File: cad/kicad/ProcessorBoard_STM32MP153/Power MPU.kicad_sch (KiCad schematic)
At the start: 37 parts, among them IC301 STPMIC1BPQR, J301 Conn_01x01_Pin

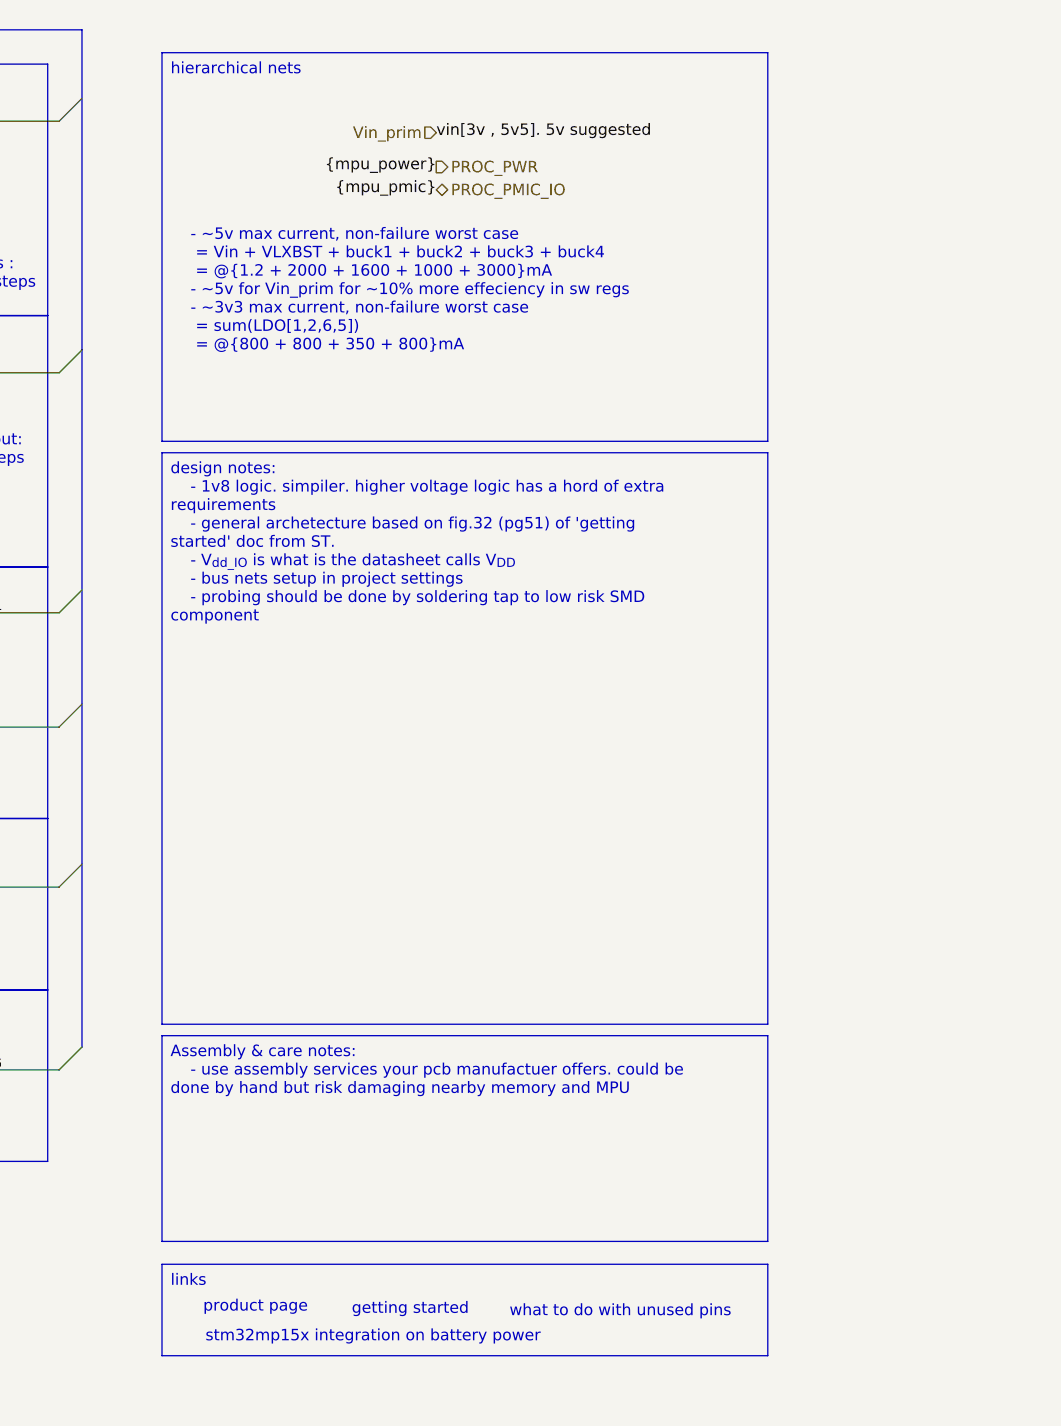
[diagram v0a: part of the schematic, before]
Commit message: realtek bridge thing somewhat more wired
apparently the proper term for via skimping and what not is NFPR (non functional pad removal). all my homies love NFPR. so it is possible to route 0.5mm bga. still fighting the dog but at least cant bring it to another layer
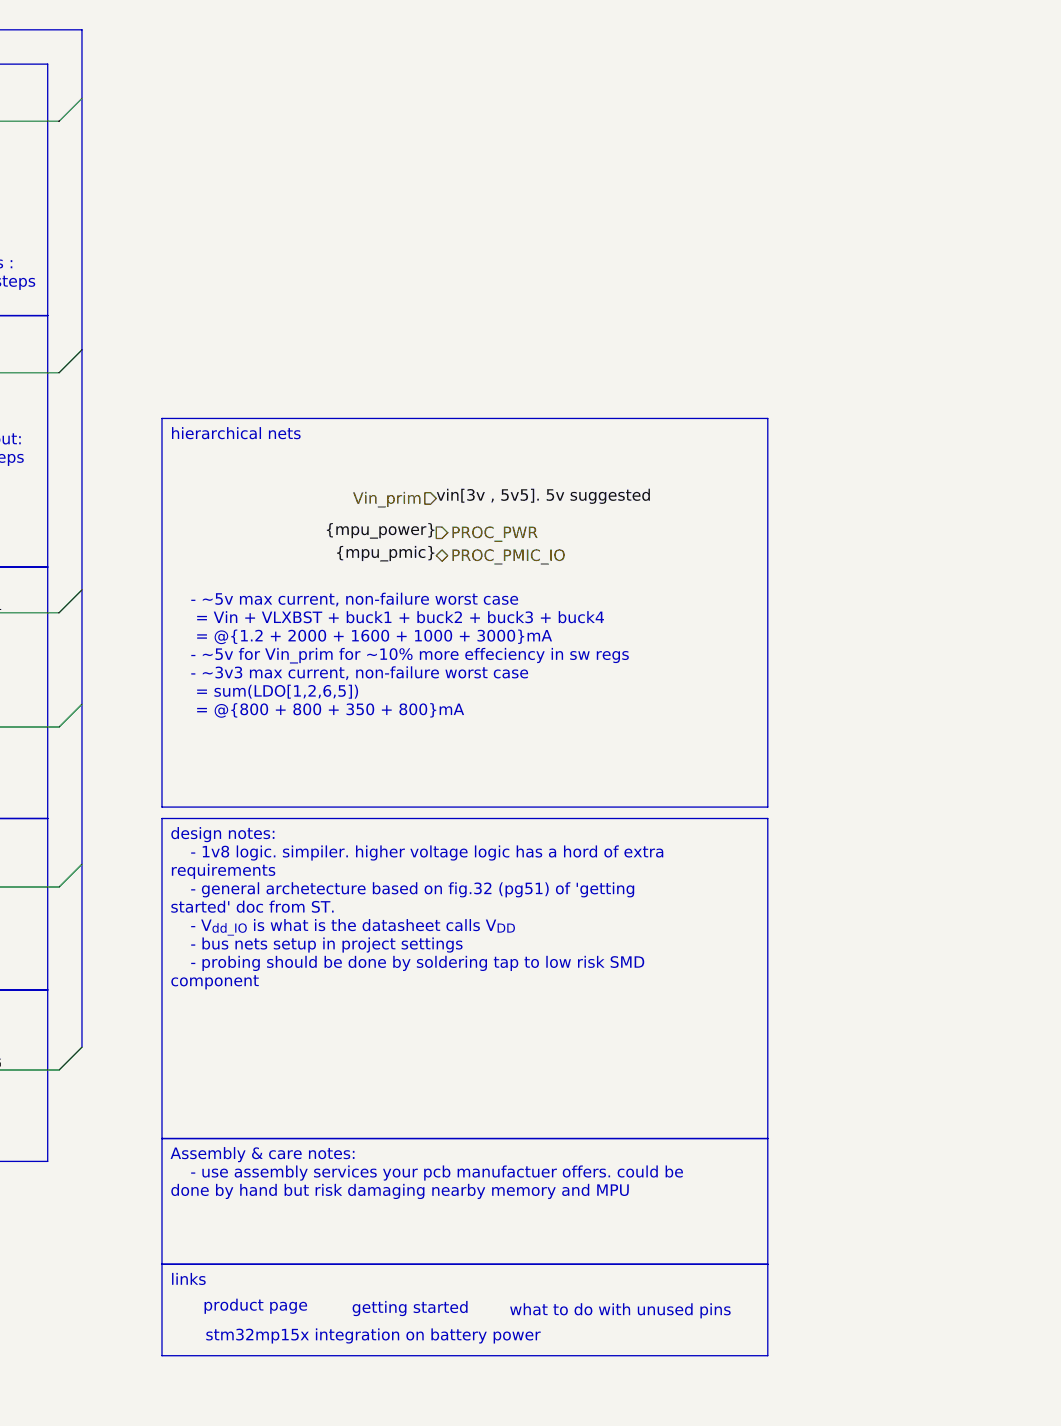
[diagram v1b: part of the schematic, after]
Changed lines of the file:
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@@
 	(text_box "Assembly & care notes:\n	- use assembly services your pcb manufactuer offers. could be done by hand but risk damaging nearby memory and MPU"
 		(exclude_from_sim no)
-		(at 215.9 128.27 0)
-		(size 67.31 22.86)
+		(at 215.9 139.7 0)
+		(size 67.31 13.97)
 		(margins 0.9398 0.9398 0.9398 0.9398)
 		(stroke
@@
 	(text_box "design notes:\n	- 1v8 logic. simpiler. higher voltage logic has a hord of extra requirements\n	- general archetecture based on fig.32 (pg51) of 'getting started' doc from ST.\n	- V_{dd_IO} is what is the datasheet calls V_{DD}\n	- bus nets setup in project settings\n	- probing should be done by soldering tap to low risk SMD component\n"
 		(exclude_from_sim no)
-		(at 215.9 63.5 0)
-		(size 67.31 63.5)
+		(at 215.9 104.14 0)
+		(size 67.31 35.56)
 		(margins 0.9398 0.9398 0.9398 0.9398)
 		(stroke
@@
 	(text_box "hierarchical nets\n\n\n\n\n\n\n\n\n	- ~5v max current, non-failure worst case\n	 = Vin + VLXBST + buck1 + buck2 + buck3 + buck4\n	 = @{1.2 + 2000 + 1600 + 1000 + 3000}mA\n	- ~5v for Vin_prim for ~10% more effeciency in sw regs\n	- ~3v3 max current, non-failure worst case\n	 = sum(LDO[1,2,6,5])\n	 = @{800 + 800 + 350 + 800}mA"
 		(exclude_from_sim no)
-		(at 215.9 19.05 0)
+		(at 215.9 59.69 0)
 		(size 67.31 43.18)
 		(margins 0.9525 0.9525 0.9525 0.9525)
@@
 	)
 	(image
-		(at 248.92 119.38)
+		(at 248.92 132.08)
 		(data "iVBORw0KGgoAAAANSUhEUgAAAukAAACPCAYAAABH9kVlAAAABHNCSVQICAgIfAhkiAAAIABJREFU"
 			"eJztnX14XFd957/jdycxpMSUGALR1bKhI6RN5JZ40w1QEwLoipQgai+aqVRAadNAX4AZaR0ekw2p"
@@
 	)
 	(label "{mpu_pmic}"
-		(at 246.38 34.29 180)
+		(at 246.38 74.93 180)
 		(effects
 			(font
@@
 	)
 	(label "{mpu_power}"
-		(at 246.38 31.75 180)
+		(at 246.38 72.39 180)
 		(effects
 			(font
@@
 	)
 	(label "vin[3v , 5v5]. 5v suggested"
-		(at 246.38 27.94 0)
+		(at 246.38 68.58 0)
 		(effects
 			(font
@@
 	(hierarchical_label "PROC_PWR"
 		(shape output)
-		(at 246.38 31.75 0)
+		(at 246.38 72.39 0)
 		(effects
 			(font
@@
 	(hierarchical_label "PROC_PMIC_IO"
 		(shape bidirectional)
-		(at 246.38 34.29 0)
+		(at 246.38 74.93 0)
 		(effects
 			(font
@@
 	(hierarchical_label "Vin_prim"
 		(shape input)
-		(at 246.38 27.94 180)
+		(at 246.38 68.58 180)
 		(effects
 			(font
@@
 					(unit 1)
 				)
-				(path "/e63e39d7-6ac0-4ffd-8aa3-1841a4541b55/81050333-713e-43ae-813a-57b604ffaa46"
-					(reference "NT1101")
-					(unit 1)
-				)
 			)
 		)
@@
 					(unit 1)
 				)
-				(path "/e63e39d7-6ac0-4ffd-8aa3-1841a4541b55/81050333-713e-43ae-813a-57b604ffaa46"
-					(reference "C1117")
-					(unit 1)
-				)
 			)
 		)
@@
 					(unit 1)
 				)
-				(path "/e63e39d7-6ac0-4ffd-8aa3-1841a4541b55/81050333-713e-43ae-813a-57b604ffaa46"
-					(reference "L1103")
-					(unit 1)
-				)
 			)
 		)
@@
 					(unit 1)
 				)
-				(path "/e63e39d7-6ac0-4ffd-8aa3-1841a4541b55/81050333-713e-43ae-813a-57b604ffaa46"
-					(reference "C1113")
-					(unit 1)
-				)
 			)
 		)
@@
 					(unit 1)
 				)
-				(path "/e63e39d7-6ac0-4ffd-8aa3-1841a4541b55/81050333-713e-43ae-813a-57b604ffaa46"
-					(reference "NT1102")
-					(unit 1)
-				)
 			)
 		)
@@
 					(unit 1)
 				)
-				(path "/e63e39d7-6ac0-4ffd-8aa3-1841a4541b55/81050333-713e-43ae-813a-57b604ffaa46"
-					(reference "J1101")
-					(unit 1)
-				)
 			)
 		)
@@
 					(unit 1)
 				)
-				(path "/e63e39d7-6ac0-4ffd-8aa3-1841a4541b55/81050333-713e-43ae-813a-57b604ffaa46"
-					(reference "C1121")
-					(unit 1)
-				)
 			)
 		)
@@
 					(unit 1)
 				)
-				(path "/e63e39d7-6ac0-4ffd-8aa3-1841a4541b55/81050333-713e-43ae-813a-57b604ffaa46"
-					(reference "C1122")
-					(unit 1)
-				)
 			)
 		)
@@
 					(unit 1)
 				)
-				(path "/e63e39d7-6ac0-4ffd-8aa3-1841a4541b55/81050333-713e-43ae-813a-57b604ffaa46"
-					(reference "C1120")
-					(unit 1)
-				)
 			)
 		)
@@
 					(unit 1)
 				)
-				(path "/e63e39d7-6ac0-4ffd-8aa3-1841a4541b55/81050333-713e-43ae-813a-57b604ffaa46"
-					(reference "C1101")
-					(unit 1)
-				)
 			)
 		)
@@
 					(unit 1)
 				)
-				(path "/e63e39d7-6ac0-4ffd-8aa3-1841a4541b55/81050333-713e-43ae-813a-57b604ffaa46"
-					(reference "L1101")
-					(unit 1)
-				)
 			)
 		)
@@
 					(unit 1)
 				)
-				(path "/e63e39d7-6ac0-4ffd-8aa3-1841a4541b55/81050333-713e-43ae-813a-57b604ffaa46"
-					(reference "C1105")
-					(unit 1)
-				)
 			)
 		)
@@
 					(unit 1)
 				)
-				(path "/e63e39d7-6ac0-4ffd-8aa3-1841a4541b55/81050333-713e-43ae-813a-57b604ffaa46"
-					(reference "C1110")
-					(unit 1)
-				)
 			)
 		)
@@
 					(unit 1)
 				)
-				(path "/e63e39d7-6ac0-4ffd-8aa3-1841a4541b55/81050333-713e-43ae-813a-57b604ffaa46"
-					(reference "C1107")
-					(unit 1)
-				)
 			)
 		)
@@
 					(unit 1)
 				)
-				(path "/e63e39d7-6ac0-4ffd-8aa3-1841a4541b55/81050333-713e-43ae-813a-57b604ffaa46"
-					(reference "C1104")
-					(unit 1)
-				)
 			)
 		)
@@
 					(unit 1)
 				)
-				(path "/e63e39d7-6ac0-4ffd-8aa3-1841a4541b55/81050333-713e-43ae-813a-57b604ffaa46"
-					(reference "NT1103")
-					(unit 1)
-				)
 			)
 		)
@@
 					(unit 1)
 				)
-				(path "/e63e39d7-6ac0-4ffd-8aa3-1841a4541b55/81050333-713e-43ae-813a-57b604ffaa46"
-					(reference "C1116")
-					(unit 1)
-				)
 			)
 		)
@@
 					(unit 1)
 				)
-				(path "/e63e39d7-6ac0-4ffd-8aa3-1841a4541b55/81050333-713e-43ae-813a-57b604ffaa46"
-					(reference "R1102")
-					(unit 1)
-				)
 			)
 		)
@@
 					(unit 1)
 				)
-				(path "/e63e39d7-6ac0-4ffd-8aa3-1841a4541b55/81050333-713e-43ae-813a-57b604ffaa46"
-					(reference "C1123")
-					(unit 1)
-				)
 			)
 		)
@@
 					(unit 1)
 				)
-				(path "/e63e39d7-6ac0-4ffd-8aa3-1841a4541b55/81050333-713e-43ae-813a-57b604ffaa46"
-					(reference "C1115")
-					(unit 1)
-				)
 			)
 		)
@@
 					(unit 1)
 				)
-				(path "/e63e39d7-6ac0-4ffd-8aa3-1841a4541b55/81050333-713e-43ae-813a-57b604ffaa46"
-					(reference "C1111")
-					(unit 1)
-				)
 			)
 		)
@@
 					(unit 1)
 				)
-				(path "/e63e39d7-6ac0-4ffd-8aa3-1841a4541b55/81050333-713e-43ae-813a-57b604ffaa46"
-					(reference "#PWR01101")
-					(unit 1)
-				)
 			)
 		)
@@
 					(unit 1)
 				)
-				(path "/e63e39d7-6ac0-4ffd-8aa3-1841a4541b55/81050333-713e-43ae-813a-57b604ffaa46"
-					(reference "NT1104")
-					(unit 1)
-				)
 			)
 		)
@@
 					(unit 1)
 				)
-				(path "/e63e39d7-6ac0-4ffd-8aa3-1841a4541b55/81050333-713e-43ae-813a-57b604ffaa46"
-					(reference "C1118")
-					(unit 1)
-				)
 			)
 		)
@@
 					(unit 1)
 				)
-				(path "/e63e39d7-6ac0-4ffd-8aa3-1841a4541b55/81050333-713e-43ae-813a-57b604ffaa46"
-					(reference "C1103")
-					(unit 1)
-				)
 			)
 		)
@@
 					(unit 1)
 				)
-				(path "/e63e39d7-6ac0-4ffd-8aa3-1841a4541b55/81050333-713e-43ae-813a-57b604ffaa46"
-					(reference "C1109")
-					(unit 1)
-				)
 			)
 		)
@@
 					(unit 1)
 				)
-				(path "/e63e39d7-6ac0-4ffd-8aa3-1841a4541b55/81050333-713e-43ae-813a-57b604ffaa46"
-					(reference "C1124")
-					(unit 1)
-				)
 			)
 		)
@@
 					(unit 1)
 				)
-				(path "/e63e39d7-6ac0-4ffd-8aa3-1841a4541b55/81050333-713e-43ae-813a-57b604ffaa46"
-					(reference "L1104")
-					(unit 1)
-				)
 			)
 		)
@@
 					(unit 1)
 				)
-				(path "/e63e39d7-6ac0-4ffd-8aa3-1841a4541b55/81050333-713e-43ae-813a-57b604ffaa46"
-					(reference "R1101")
-					(unit 1)
-				)
 			)
 		)
@@
 					(unit 1)
 				)
-				(path "/e63e39d7-6ac0-4ffd-8aa3-1841a4541b55/81050333-713e-43ae-813a-57b604ffaa46"
-					(reference "L1102")
-					(unit 1)
-				)
 			)
 		)
@@
 					(unit 1)
 				)
-				(path "/e63e39d7-6ac0-4ffd-8aa3-1841a4541b55/81050333-713e-43ae-813a-57b604ffaa46"
-					(reference "C1119")
-					(unit 1)
-				)
 			)
 		)
@@
 					(unit 1)
 				)
-				(path "/e63e39d7-6ac0-4ffd-8aa3-1841a4541b55/81050333-713e-43ae-813a-57b604ffaa46"
-					(reference "C1112")
-					(unit 1)
-				)
 			)
 		)
@@
 					(unit 1)
 				)
-				(path "/e63e39d7-6ac0-4ffd-8aa3-1841a4541b55/81050333-713e-43ae-813a-57b604ffaa46"
-					(reference "C1108")
-					(unit 1)
-				)
 			)
 		)
@@
 					(unit 1)
 				)
-				(path "/e63e39d7-6ac0-4ffd-8aa3-1841a4541b55/81050333-713e-43ae-813a-57b604ffaa46"
-					(reference "IC1101")
-					(unit 1)
-				)
 			)
 		)
@@
 					(unit 1)
 				)
-				(path "/e63e39d7-6ac0-4ffd-8aa3-1841a4541b55/81050333-713e-43ae-813a-57b604ffaa46"
-					(reference "C1114")
-					(unit 1)
-				)
 			)
 		)
@@
 					(unit 1)
 				)
-				(path "/e63e39d7-6ac0-4ffd-8aa3-1841a4541b55/81050333-713e-43ae-813a-57b604ffaa46"
-					(reference "L1105")
-					(unit 1)
-				)
 			)
 		)
@@
 					(unit 1)
 				)
-				(path "/e63e39d7-6ac0-4ffd-8aa3-1841a4541b55/81050333-713e-43ae-813a-57b604ffaa46"
-					(reference "C1102")
-					(unit 1)
-				)
 			)
 		)
@@
 					(unit 1)
 				)
-				(path "/e63e39d7-6ac0-4ffd-8aa3-1841a4541b55/81050333-713e-43ae-813a-57b604ffaa46"
-					(reference "C1106")
-					(unit 1)
-				)

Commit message: miled fixes
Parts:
- added C325: 100n, Capacitor_SMD:C_0402_1005Metric_Pad0.74x0.62mm_HandSolder, symbol Device:C_Small
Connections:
- net GND: now also C325.1
- net V_{DDR_ref}: now also C325.2
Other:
- moved on the sheet: C320, R301, R302
